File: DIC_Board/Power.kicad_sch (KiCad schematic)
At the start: 0 parts

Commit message: Complete MCU and regulated power schematics
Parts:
- added C100: 100uF, Capacitor_SMD:CP_Elec_8x10.5, symbol Device:C
- added C101, C102, C103: 100nF, Capacitor_SMD:C_0402_1005Metric, symbol Device:C
- added C104: 10nF, Capacitor_SMD:C_0402_1005Metric, symbol Device:C
- added C105: 100 pF C0G, Capacitor_SMD:C_0402_1005Metric, symbol Device:C
- added C106: 4.7 uF 16 V, Capacitor_SMD:C_0603_1608Metric, symbol Device:C
- added C107, C108: 10uF, Capacitor_SMD:C_1206_3216Metric, symbol Device:C
- added C109, C110, C111, C112: 22 uF 25 V, Capacitor_SMD:C_1210_3225Metric, symbol Device:C
- added C113: 100 uF 25 V, Capacitor_SMD:CP_Elec_8x10.5, symbol Device:C
- added C114: 1 uF 10 V, Capacitor_SMD:C_0603_1608Metric, symbol Device:C
- added C115, C116: 10 uF 50 V, Capacitor_SMD:C_1206_3216Metric, symbol Device:C
- added C117, C118: 47 uF 10 V, Capacitor_SMD:C_1210_3225Metric, symbol Device:C
- added D10: SMBJ18A, Diode_SMD:D_SMB, symbol Device:D_TVS
- added F10: 6A, Fuse:Fuse_Littelfuse-NANO2-451_453, symbol Device:Fuse
- added L10: 4.7uH, Inductor_SMD:L_Coilcraft_XAL7070-XXX, symbol Device:L
- added R100: 150 k 1%, Resistor_SMD:R_0402_1005Metric, symbol Device:R
- added R101: 24.9 k 1%, Resistor_SMD:R_0402_1005Metric, symbol Device:R
- added R102: 49.9k, Resistor_SMD:R_0402_1005Metric, symbol Device:R
- added R103: 16.5 mOhm 1 W, Resistor_SMD:R_2512_6332Metric, symbol Device:R
- added R104: 100 k 1%, Resistor_SMD:R_0402_1005Metric, symbol Device:R
- added R105: 11.1 k 1%, Resistor_SMD:R_0402_1005Metric, symbol Device:R
- added R106: 49.9R, Resistor_SMD:R_0402_1005Metric, symbol Device:R
- added R107, R108, R111: 100 k, Resistor_SMD:R_0402_1005Metric, symbol Device:R
- added R109: 10 k 1%, Resistor_SMD:R_0402_1005Metric, symbol Device:R
- added R110: 4.32 k 1%, Resistor_SMD:R_0402_1005Metric, symbol Device:R
- added TP20: P_IN, TestPoint:TestPoint_Plated_Hole_D2.0mm, symbol Connector:TestPoint
- added TP21: P_IN_PROTECTED, TestPoint:TestPoint_Plated_Hole_D2.0mm, symbol Connector:TestPoint
- added TP22: +12V, TestPoint:TestPoint_Plated_Hole_D2.0mm, symbol Connector:TestPoint
- added TP23: +3V3, TestPoint:TestPoint_Plated_Hole_D2.0mm, symbol Connector:TestPoint
- added TP24: GND, TestPoint:TestPoint_Plated_Hole_D2.0mm, symbol Connector:TestPoint
- added U10: TPS552892RYQR, symbol DIC_Board:TPS552892
- added U11: TPSM53603RDAR, Package_DFN_QFN:Texas_B3QFN-14-1EP_5x5.5mm_P0.65mm_ThermalVia, symbol DIC_Board:TPSM53603RDA
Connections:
- new net: C114.1, U11.13 (V5V)
- new net: R109.2, R110.1, U11.9 (FB)
- new net: R104.2, R105.1, U10.14 (FB)
- new net: R103.1, U10.11 (VOUT), U10.12 (ISP)
- new net: C106.1, U10.18 (VCC)
- new net: R100.2, R101.2, U10.1 (EN/UVLO)
- new net: C105.1, R106.2, U10.15 (COMP)
- new net: C102.1, U10.20 (BOOT1)
- new net: R102.1, U10.6 (FSW)
- new net: C102.2, L10.1, U10.8 (SW1)
- new net: C104.1, R106.1
- new net +12V: C109.1, C110.1, C111.1, C112.1, C113.1, R103.2, R104.1, TP22.1, U10.13 (ISN)
- new net +3V3: C117.1, C118.1, R107.1, R108.1, R109.1, R111.1, TP23.1, U11.7 (VOUT), U11.8 (VOUT)
- new net 12V_OC_N: R108.2, U10.4 (CC)
- new net 12V_PG: R107.2, U10.3 (PG)
- new net 3V3_PG: R111.2, U11.6 (PGOOD)
- new net GND: C100.2, C101.2, C104.2, C105.2, C106.2, C107.2, C108.2, C109.2, C110.2, C111.2, C112.2, C113.2, C114.2, C115.2, C116.2, C117.2, C118.2, D10.1 (A1), R101.1, R102.2, R105.2, R110.2, TP24.1, U10.17 (AGND), U10.2 (MODE), U10.5 (DITH/SYNC), U10.9 (PGND), U11.10 (PGND), U11.11 (PGND), U11.12 (AGND), U11.15 (PGND), U11.3 (PGND)
- new net P_IN_PROTECTED: C100.1, C101.1, C107.1, C108.1, C115.1, C116.1, D10.2 (A2), F10.2, R100.1, TP21.1, U10.7 (VIN), U11.1 (VIN), U11.14 (VIN), U11.2 (EN)
- new net P_in: F10.1, TP20.1
- no-connect marks 0 -> 4
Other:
- note added: "- Input fuse/TVS and reverse-polarity protection remain provisional until the source is frozen."
- note added: "- Sequence analyzer warm-up, pump start, and actuator stalls; +12 V is limited to about 3 A."
- note added: "- U10 needs the checked TI RYQ0021A land pattern before PCB placement."
- note added: "DESIGN NOTES"
- note added: "POWER ENTRY"
- note added: "Provisional 9-16 V operating envelope"
- note added: "REGULATED +12 V / 3 A BUCK-BOOST"
- note added: "REGULATED +3V3 / 3 A"
- note added: "TPS552892, 400 kHz, PFM; output-current limit approximately 3 A"
- note added: "TPSM53603 step-down module, always enabled"

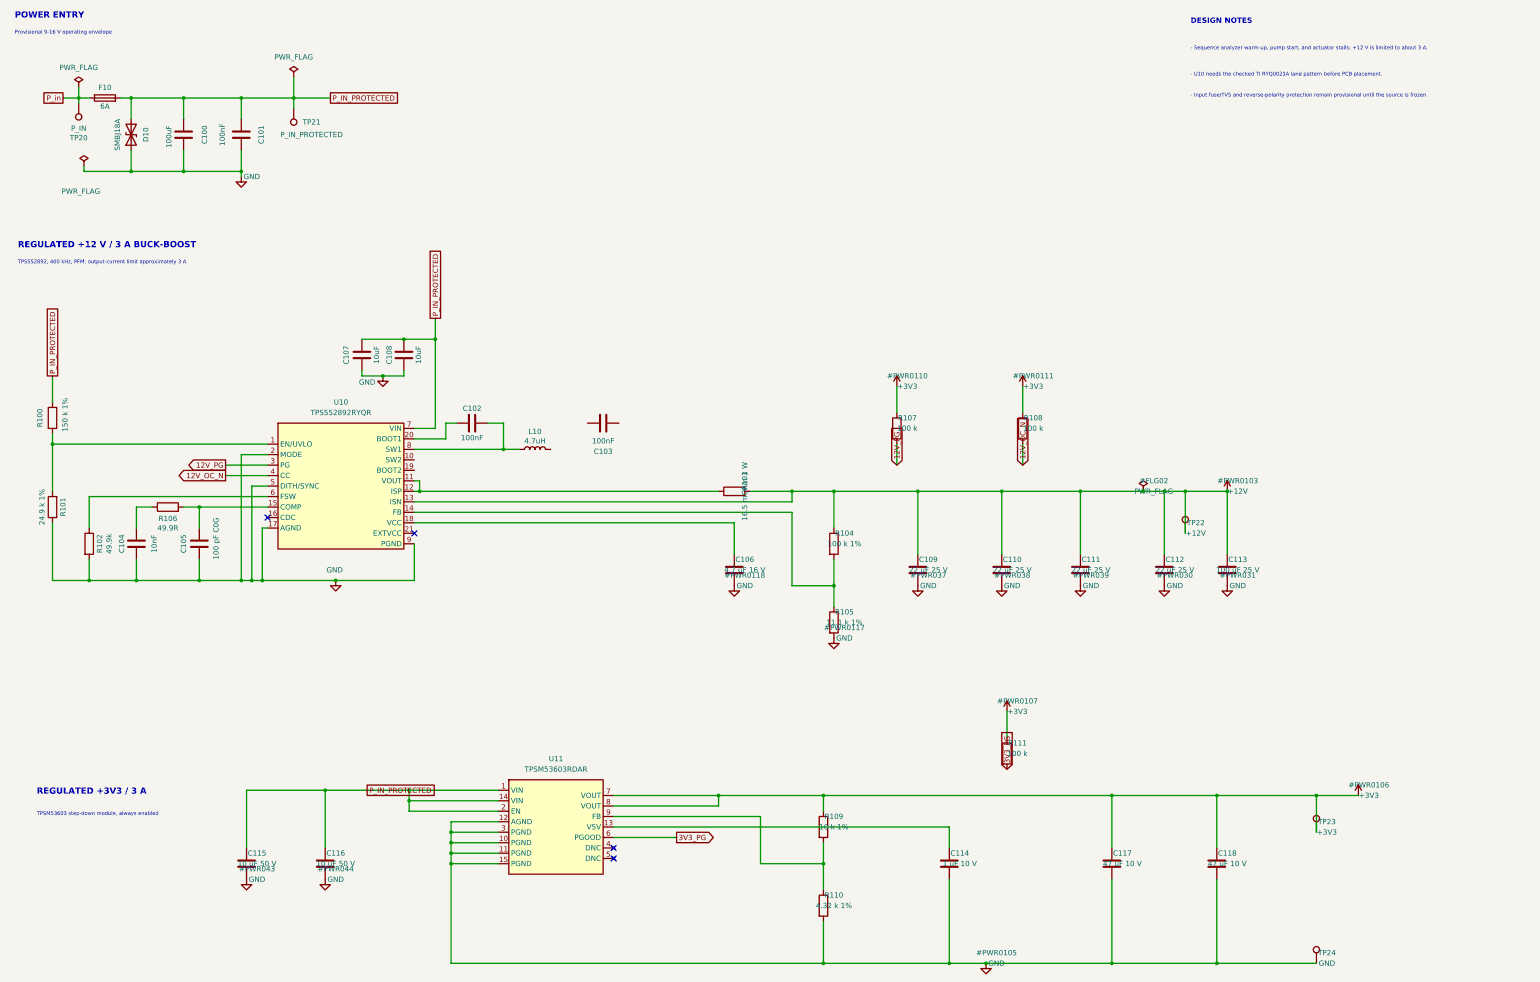
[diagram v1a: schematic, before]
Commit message: Update power supply schematic and symbol libraries
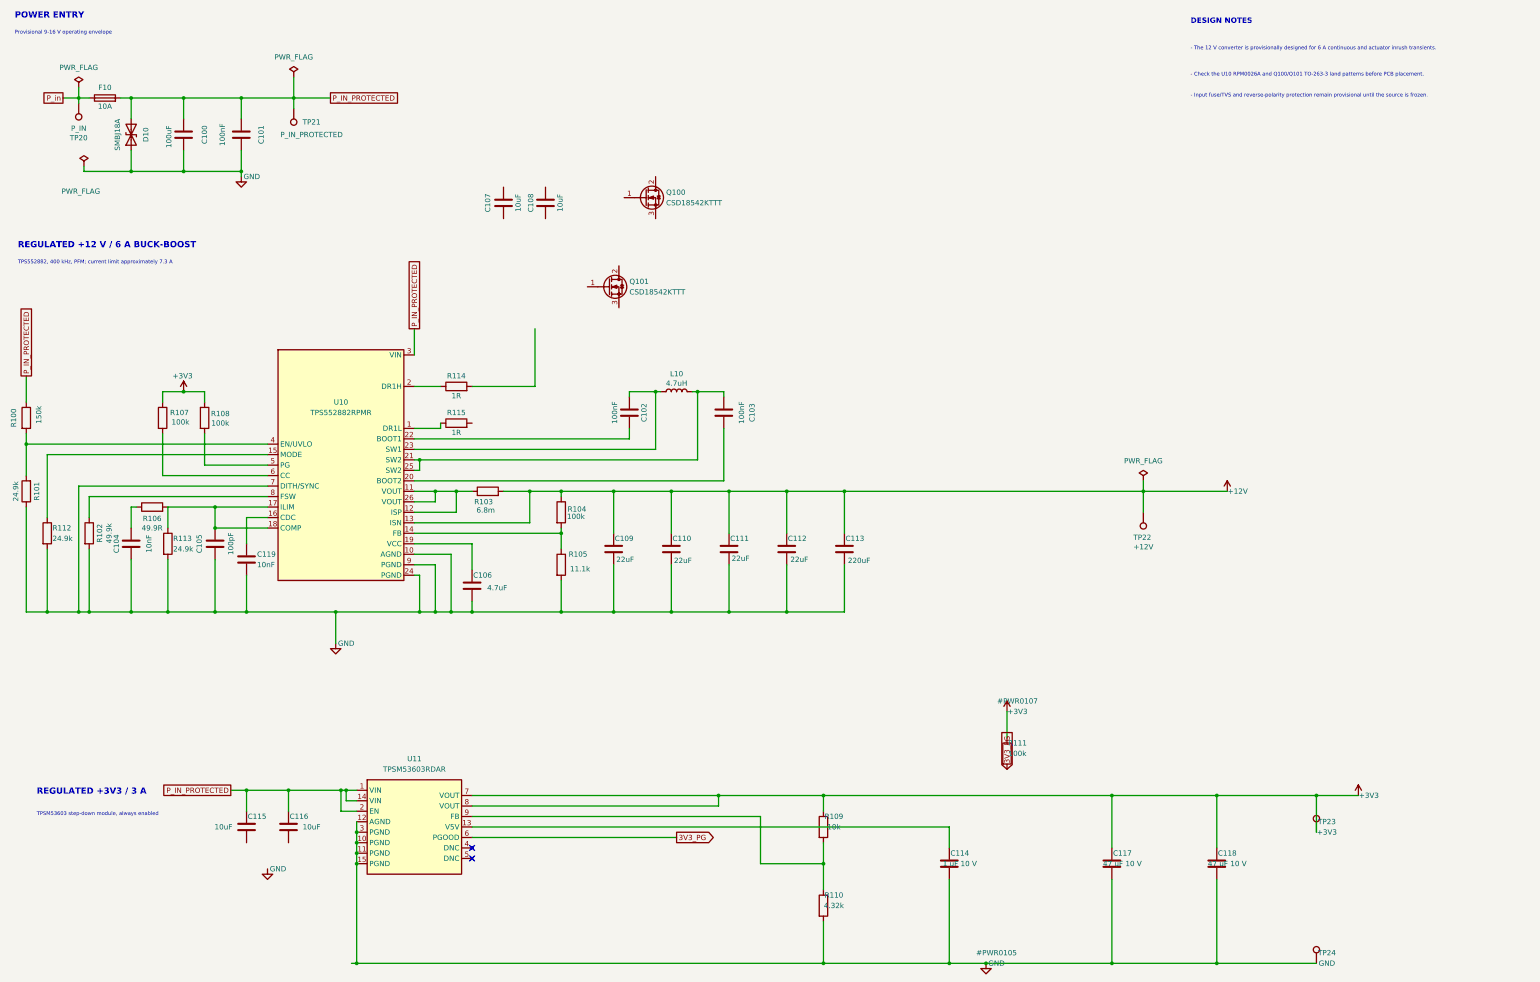
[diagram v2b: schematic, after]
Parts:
- added C119: 10nF, Capacitor_SMD:C_0402_1005Metric, symbol Device:C
- added Q100, Q101: CSD18542KTTT, Package_TO_SOT_SMD:TO-263-3_TabPin2, symbol Transistor_FET:Q_NMOS_GDS
- added R112, R113: 24.9k, Resistor_SMD:R_0402_1005Metric, symbol Device:R
- added R114, R115: 1R, Resistor_SMD:R_0603_1608Metric, symbol Device:R
- C105: value 100 pF C0G -> 100pF
- C106: value 4.7 uF 16 V -> 4.7uF
- C109, C110, C111, C112: value 22 uF 25 V -> 22uF
- C113: value 100 uF 25 V -> 220uF
- C115, C116: value 10 uF 50 V -> 10uF
- F10: value 6A -> 10A; MPN 0451006.MRL -> 0451010.MRL
- L10: footprint Inductor_SMD:L_Coilcraft_XAL7070-XXX -> Inductor_SMD:L_Coilcraft_XAL1010-XXX; MPN XAL7070-472MEB -> XAL1010-472MEB
- R100: value 150 k 1% -> 150k
- R101: value 24.9 k 1% -> 24.9k
- R103: value 16.5 mOhm 1 W -> 6.8m; MPN CSS2H-2512R-L0165F -> CSS2H-2512R-L0068F
- R104: value 100 k 1% -> 100k
- R105: value 11.1 k 1% -> 11.1k
- R107, R108, R111: value 100 k -> 100k
- R109: value 10 k 1% -> 10k
- R110: value 4.32 k 1% -> 4.32k
- U10: value TPS552892RYQR -> TPS552882RPMR; symbol DIC_Board:TPS552892 -> DIC_Board:TPS552882; MPN TPS552892RYQR -> TPS552882RPMR
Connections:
- net GND: now also U10.10 (AGND), U10.24 (PGND), U10.7 (DITH/SYNC), C119.2, R112.2, R113.2; no longer C107.2, C108.2, C115.2, C116.2, U10.17 (AGND), U10.2 (MODE), U10.5 (DITH/SYNC)
- net P_IN_PROTECTED: now also U10.3 (VIN); no longer C107.1, C108.1, U10.7 (VIN)
- net at R103.1, U10.11 (VOUT), U10.12 (ISP): now also U10.26 (VOUT)
- net at C106.1: now also U10.19 (VCC); no longer U10.18 (VCC)
- net at R100.2, R101.2: now also U10.4 (EN/UVLO); no longer U10.1 (EN/UVLO)
- net at C105.1, R106.2: now also U10.17 (ILIM), U10.18 (COMP), R113.1; no longer U10.15 (COMP)
- net at U10.16 (CDC): now also C119.1
- net at U10.20 (BOOT2): now also C103.1; no longer C102.1
- net at U10.21 (SW2): now also C103.2, L10.2, U10.25 (SW2)
- net at U10.6 (CC): now also R107.2; no longer R102.1
- net 12V_OC_N: no longer names the net of R108.2
- net 12V_OC_N: now also U10.5 (PG); no longer U10.4 (CC)
- removed net 12V_PG: R107.2, U10.3 (PG)
- new net: R112.1, U10.15 (MODE)
- new net: R115.1, U10.1 (DR1L)
- new net: R114.1, U10.2 (DR1H)
- new net: C102.2, U10.22 (BOOT1)
- new net: C102.1, L10.1, U10.23 (SW1)
- new net: R102.1, U10.8 (FSW)
- no-connect marks 4 -> 2
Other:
- note added: "- Check the U10 RPM0026A and Q100/Q101 TO-263-3 land patterns before PCB placement."
- note added: "- The 12 V converter is provisionally designed for 6 A continuous and actuator inrush transients."
- note added: "REGULATED +12 V / 6 A BUCK-BOOST"
- note added: "TPS552882, 400 kHz, PFM; current limit approximately 7.3 A"
- note removed: "- Sequence analyzer warm-up, pump start, and actuator stalls; +12 V is limited to about 3 A."
- note removed: "- U10 needs the checked TI RYQ0021A land pattern before PCB placement."
- note removed: "REGULATED +12 V / 3 A BUCK-BOOST"
- note removed: "TPS552892, 400 kHz, PFM; output-current limit approximately 3 A"
- moved on the sheet: C102, C103, C104, C105, C106, C107, C108, C109, C110, C111, C112, C113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

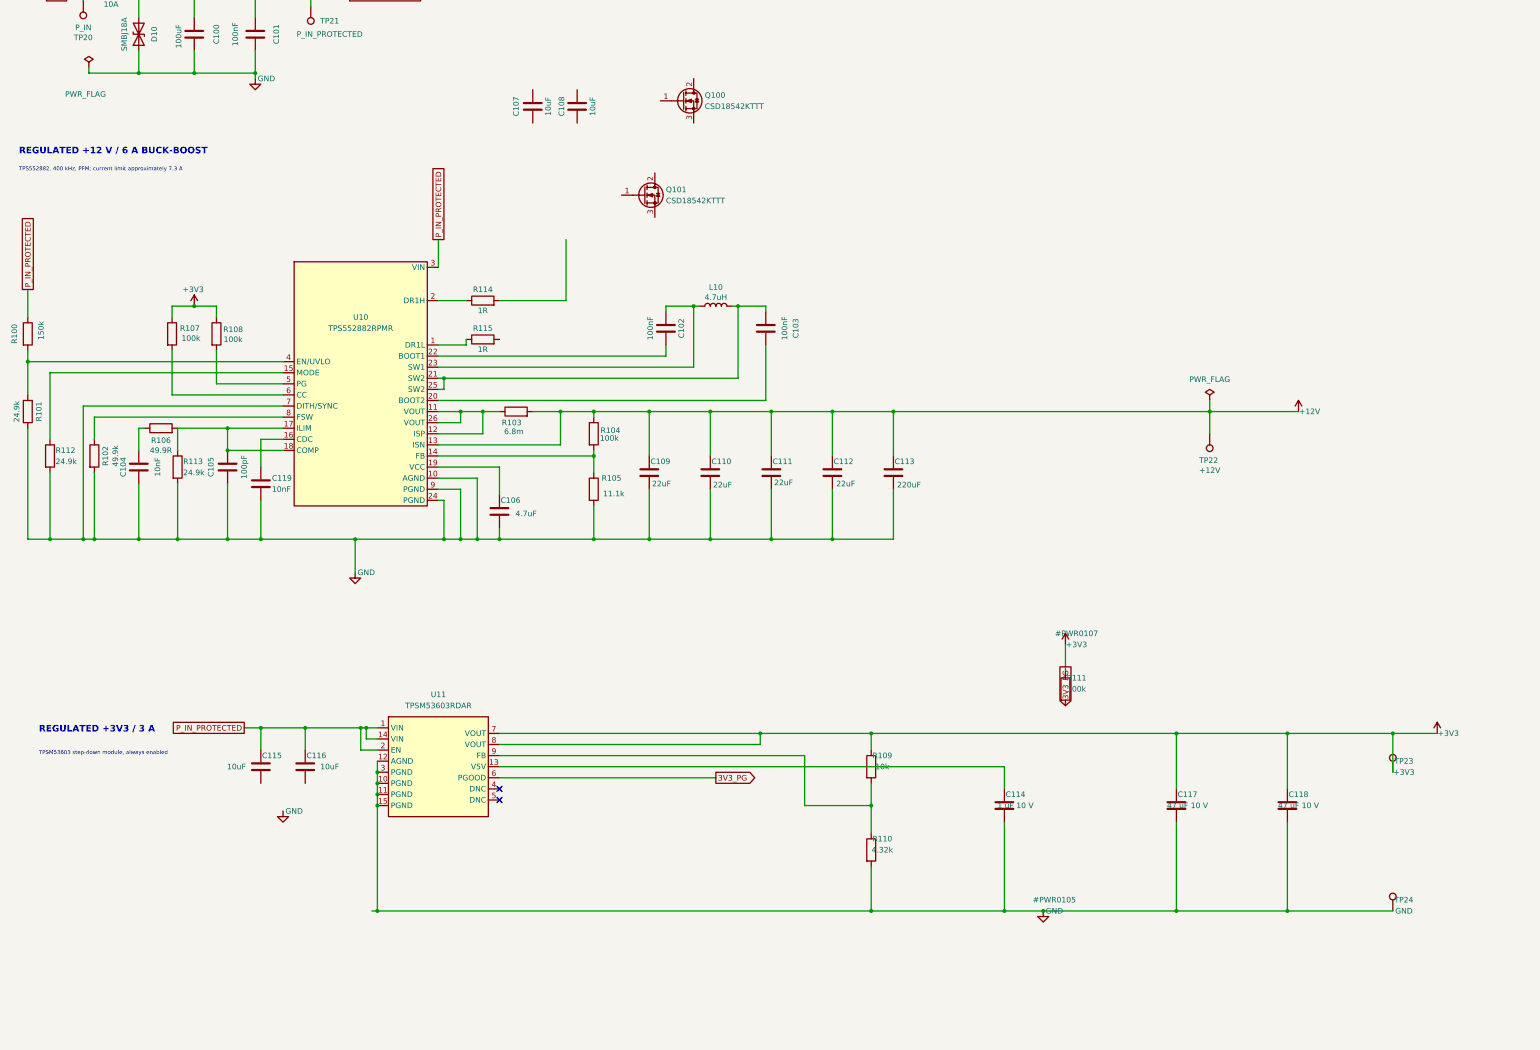
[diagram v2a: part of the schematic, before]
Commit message: Updated the 12V power circuit.
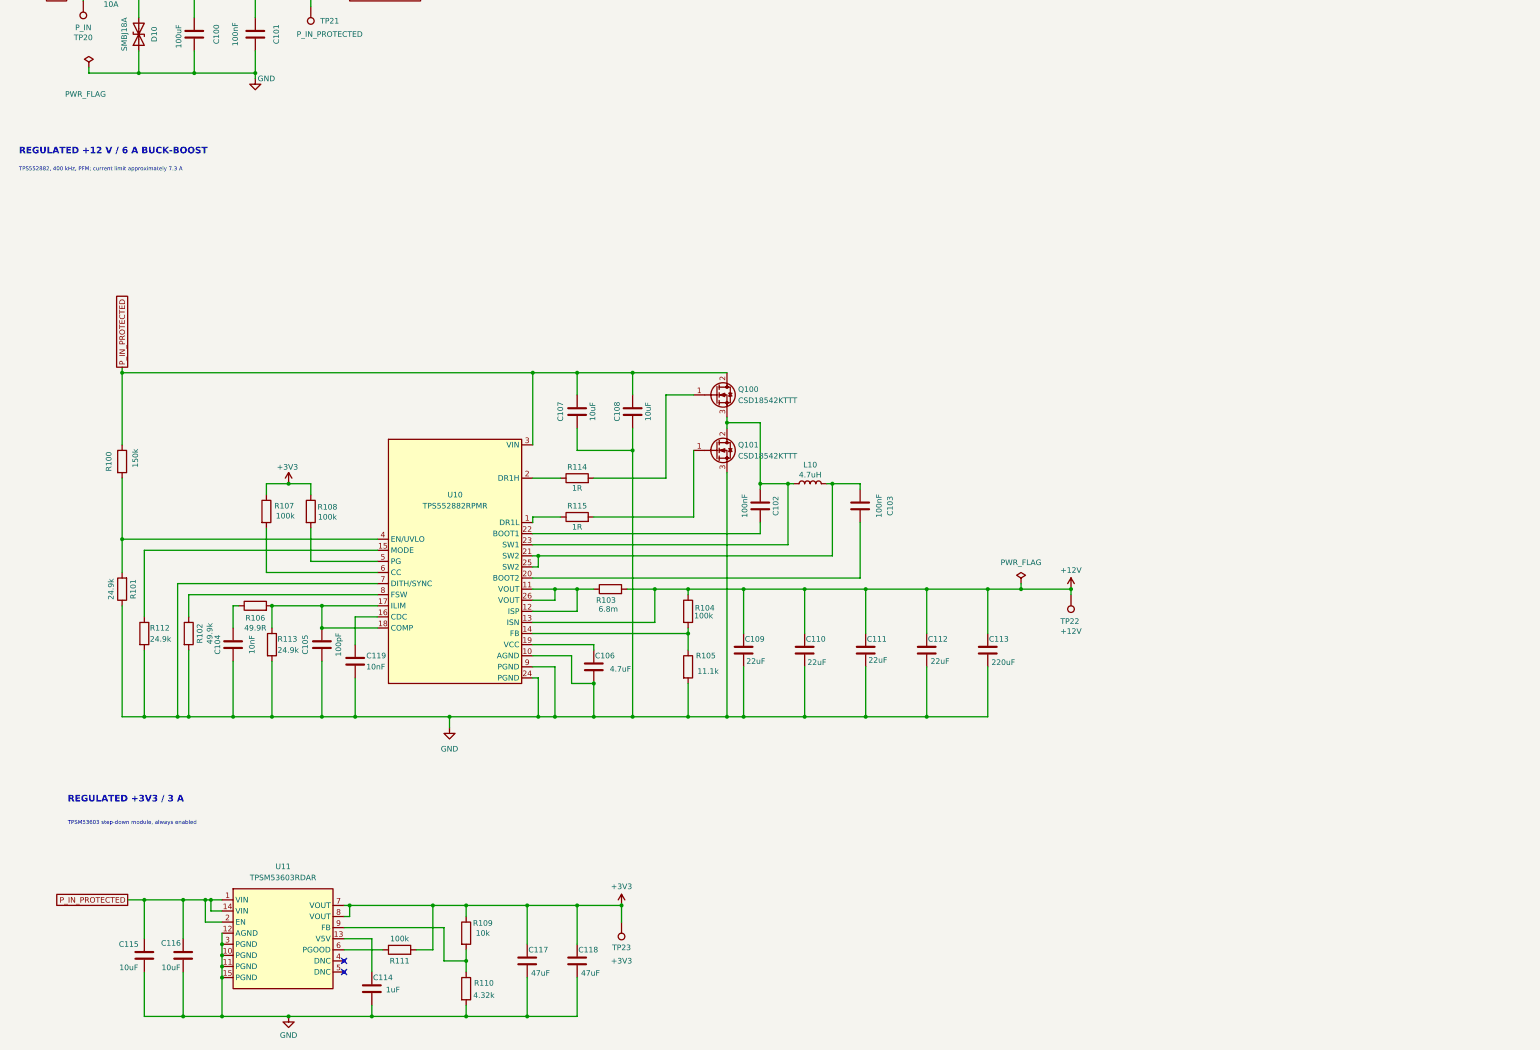
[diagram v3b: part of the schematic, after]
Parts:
- removed TP24: GND, TestPoint:TestPoint_Plated_Hole_D2.0mm, symbol Connector:TestPoint
- C114: value 1 uF 10 V -> 1uF
- C117, C118: value 47 uF 10 V -> 47uF
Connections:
- net +3V3: now also R111.2; no longer R111.1
- net GND: now also C107.2, C108.2, C115.2, C116.2, Q101.3 (S)
- net P_IN_PROTECTED: now also C107.1, C108.1, Q100.2 (D)
- net at Q101.1 (G): now also R115.2
- net at Q101.2 (D): now also C102.1, L10.1, Q100.3 (S), U10.23 (SW1)
- net at Q100.1 (G): now also R114.2
- net 3V3_PG: no longer names the net of U11.6 (PGOOD)
- net 3V3_PG: now also R111.1; no longer R111.2
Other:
- moved on the sheet: C102, C103, C104, C105, C106, C107, C108, C109, C110, C111, C112, C113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

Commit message: Fixed the 12V regulator circuit.
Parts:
- C113: MPN EEHZA1E101P -> EEHZA1E221P
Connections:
- net GND: no longer U10.7 (DITH/SYNC)
- net at C119.1: now also U10.7 (DITH/SYNC); no longer U10.16 (CDC)
- no-connect marks 2 -> 3
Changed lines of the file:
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@@
 	)
 	(junction
-		(at 52.07 200.66)
-		(diameter 0)
-		(color 0 0 0 0)
-	)
-	(junction
 		(at 73.66 175.26)
 		(diameter 0)
@@
 		(at 90.17 259.08)
 	)
+	(no_connect
+		(at 97.79 177.8)
+	)
 	(wire
 		(pts
@@
 	(wire
 		(pts
-			(xy 54.61 200.66) (xy 52.07 200.66)
+			(xy 44.45 200.66) (xy 54.61 200.66)
 		)
 		(stroke
@@
 	(wire
 		(pts
-			(xy 52.07 200.66) (xy 44.45 200.66)
-		)
-		(stroke
-			(width 0)
-			(type default)
-		)
-	)
-	(wire
-		(pts
 			(xy 92.71 200.66) (xy 85.09 200.66)
 		)
@@
 	(wire
 		(pts
-			(xy 97.79 177.8) (xy 92.71 177.8)
-		)
-		(stroke
-			(width 0)
-			(type default)
-		)
-	)
-	(wire
-		(pts
-			(xy 92.71 177.8) (xy 92.71 184.15)
-		)
-		(stroke
-			(width 0)
-			(type default)
-		)
-	)
-	(wire
-		(pts
 			(xy 92.71 191.77) (xy 92.71 200.66)
 		)
@@
 	(wire
 		(pts
+			(xy 92.71 170.18) (xy 97.79 170.18)
+		)
+		(stroke
+			(width 0)
+			(type default)
+		)
+	)
+	(wire
+		(pts
 			(xy 133.35 186.69) (xy 142.24 186.69)
 		)
@@
 	(wire
 		(pts
-			(xy 52.07 170.18) (xy 97.79 170.18)
+			(xy 73.66 200.66) (xy 64.77 200.66)
 		)
 		(stroke
@@
 	(wire
 		(pts
-			(xy 73.66 200.66) (xy 64.77 200.66)
+			(xy 44.45 242.57) (xy 44.45 251.46)
 		)
 		(stroke
@@
 	(wire
 		(pts
-			(xy 44.45 242.57) (xy 44.45 251.46)
+			(xy 92.71 170.18) (xy 92.71 184.15)
 		)
 		(stroke
@@
 	(wire
 		(pts
-			(xy 52.07 170.18) (xy 52.07 200.66)
-		)
-		(stroke
-			(width 0)
-			(type default)
-		)
-	)
-	(wire
-		(pts
 			(xy 132.08 269.24) (xy 143.51 269.24)
 		)
@@
 			)
 		)
-		(property "MPN" "EEHZA1E101P"
+		(property "MPN" "EEHZA1E221P"
 			(at 237.49 185.42 0)
 			(hide yes)
